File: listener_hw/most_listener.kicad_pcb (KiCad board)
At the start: 2 copper layers, 125 x 80 mm, 169 parts, among them J1 1-1394640-1, J2 ANALYSER, J3 I2S, J4 VBAT_IN, J5 PLR135/T10, J6 PLT133/T10W, J7 RCA 75R, J8 LINE L, J9 LINE R, M1 Tang Nano 20K, M2 ESP32-DevKitC-VIE, U1 74LVC1G34, U10 TPS2553DBVR, U11 74LVC1G123, U12 DIR9001, U13 SRC4192, U14 LP5907MFX-3.3, U15 PCM5102A, U16 LP5907MFX-3.3, U17 OPA1678, U18 TPS60403, U2 74LVC1G157, U3 74LVC1G125, U4 74LVC1G123, U5 TPS7B8133DRV, U6 LMR38020F, U7 Si514, U8 LP5907MFX-3.3, U9 74LVC1G79, X1 24.576MHz

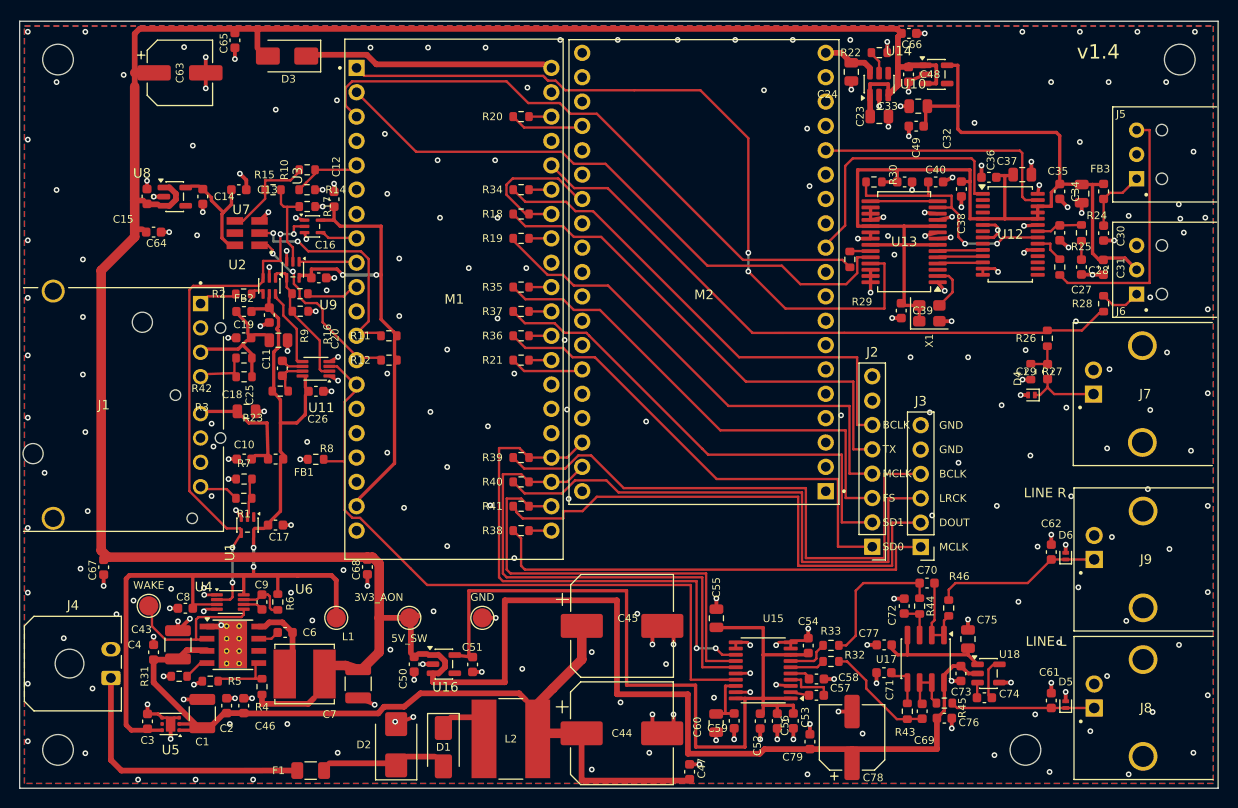
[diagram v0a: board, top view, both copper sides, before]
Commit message: Board v1.4 polished: 6 jumpers (was 9), the user's re-placement routed by hand
The user re-placed 57 parts in rounds: the DIR9001 group packed into three
columns, J2/J3 moved with their bus, the line-out buffer and the power corner
tightened, then R29, R30, R38, R40 and R41. Every net they touched was redrawn
by hand; the autorouter's first pass (25 jumpers) was dropped.

Three jumpers went with it:
- SRC_BCLK: R29 sits where the line crossed under M2, and it runs between its
  pads.
- RST_AIN: from U13.13 through U13's body and under C39/X1 into U12's body.
  U13's 3.3 V links moved outside its body (pins 19/22 left, 10/7 right, C39/X1
  fed from pin 7).
- I2S_BCLK: R39 under M2 by M2.22. The DAC's BCLK comes down through the bodies
  of R40/R41/R38 on top of its bundle, so U15 gets BCLK, DOUT, LRCK in its own
  order.
The U7 knot keeps its three hops, shorter: RX_BUF at the top of its legs,
SI_SCL straight, SI_SDA 1.3 mm.

TP4 (WAKE) is gone from the sheet, the board and gen_listener_pcb.py; WAKE is
probed at R31 or U4. The DevKitC footprint's courtyard is its two pin rows and
the antenna's end: the module sits on headers with room under it.

Board: 6 jumpers, 14 mm of bottom copper, DRC 0/0/0 with schematic parity, ERC
clean. README, the sheet PDF and the fab package follow; sheet and board are
dated 2026-10-02.

Co-Authored-By: Claude Opus 5.5 <noreply@anthropic.com>
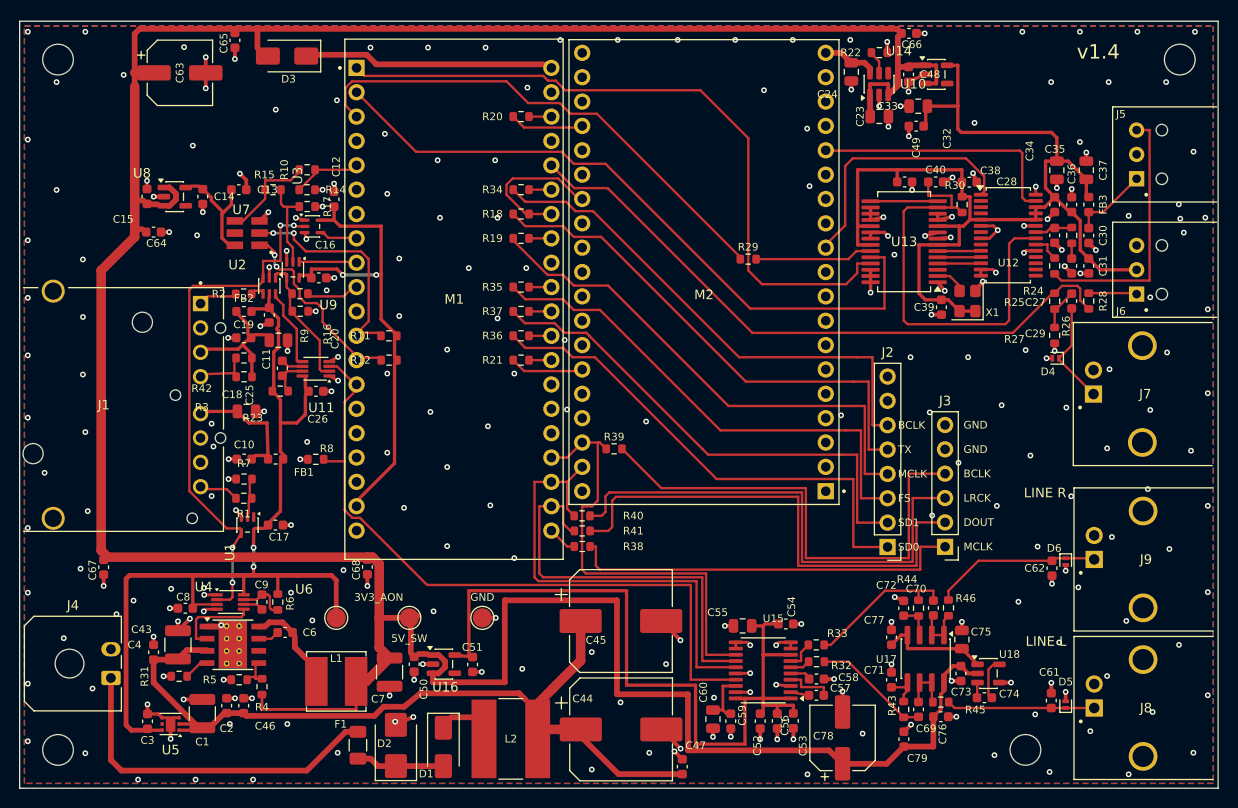
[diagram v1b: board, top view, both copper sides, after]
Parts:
- removed TP4: WAKE, TestPoint:TestPoint_Pad_D2.0mm
- moved R29 10.6 mm to (76.0, 24.8), turned to 180 degrees
- moved C79 9.81 mm to (92.2, 74.9)
- moved R39 9.74 mm to (62.0, 44.6), turned to 0 degrees
- moved R30 9.49 mm to (98.3, 19.1), turned to -90 degrees
- moved C36 9.09 mm to (109.7, 19.1), turned to 90 degrees
- moved C29 7.78 mm to (109.7, 29.2)
- moved R40 7.28 mm to (58.7, 51.6), turned to 0 degrees
- moved R41 6.87 mm to (58.7, 53.2), turned to 0 degrees
- moved C37 6.70 mm to (111.3, 15.5), turned to 90 degrees
- moved R38 6.59 mm to (58.7, 54.8), turned to 0 degrees
- moved F1 5.59 mm to (35.3, 75.5), turned to -90 degrees
- moved D4 4.59 mm to (108.1, 35.2)
- moved R27 4.53 mm to (108.0, 32.8)
- moved C39 4.21 mm to (96.1, 29.8)
- moved X1 4.18 mm to (98.9, 29.2), turned to 90 degrees
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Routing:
- net /RST_AIN: track 26.7 -> 45.3 mm, vias 2 -> 0
- net /I2S_DIN2_F: track 64.4 -> 52.7 mm
- net Net-(U13-SDOUT): track 2.16 -> 12.3 mm
- net Net-(J3-BCLK): track 61.0 -> 51.5 mm
- net /I2S_BCLK_F: track 55.3 -> 45.9 mm, vias 2 -> 0
- net 5V_SW: track 316.4 -> 325.0 mm
- net Net-(J4-VBAT): track 28.4 -> 36.5 mm
- net /WAKE: track 16.5 -> 8.89 mm
- net /SRC_BCLK_F: track 78.6 -> 71.4 mm, vias 2 -> 0
- net /SRC_LRCK_F: track 64.0 -> 71.2 mm
- net 3V3_DA: track 118.5 -> 111.8 mm
- net Net-(J3-MCLK): track 48.2 -> 41.6 mm
- net Net-(J3-LRCK): track 58.0 -> 52.9 mm
- net GND: track 148.3 -> 143.5 mm, vias 275 -> 268
- net 3V3_DAC: track 88.4 -> 84.1 mm
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
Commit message: Board v1.4: 4 jumpers (was 6), the user's last re-placement and the Si514 knot sketch
The user moved the battery corner (F1 by J4, U5 up by U4, L2/D1/D2 left, C43/C2/C46
turned to face U6), U10 and U14 with their capacitors, J2 and J3, and the DAC (U15 and
its capacitors higher, U16 with C50/C51 beside U15, so 3V3_DAC is a short spine under
U15's body); everything re-routed by hand.

- Si514 corner, the user's sketch: RT_CLK takes one jumper under RX_BUF and SI_SCL;
  RX_BUF runs between the Si514's pad rows and over it, CLK+ round its west side, so
  the RX_BUF, SI_SCL and SI_SDA jumpers are gone. SI_SCL dips under 3V3_SW at M1's
  row instead of 3V3_SW jumping SI_SCL.
- C80 (100n), C81 (100u 16V) and C82 (100n 100V): the user's copies on the board, now
  in the sheet; J4's ground stub is shorter so the VBAT_P row takes C82.
- Every junction is a shared vertex; the moved parts' labels are re-placed and J2/J3's
  pin names follow the headers again.

DRC 0 errors, 0 unconnected, 0 differences from the sheet; ERC clean; the copper lint
shows only its accepted set. Sheet PDF and fab/ re-made.

Co-Authored-By: Claude Opus 5.5 <noreply@anthropic.com>
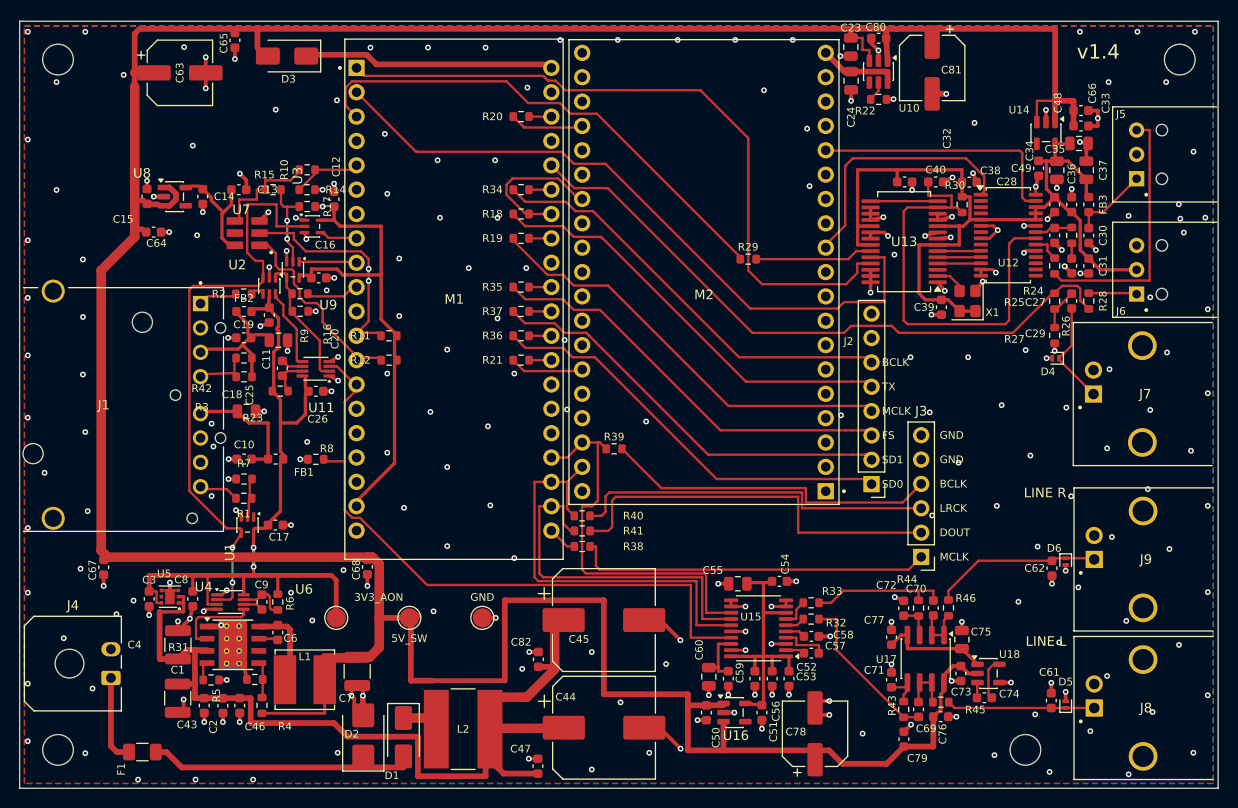
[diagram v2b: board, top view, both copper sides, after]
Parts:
- added C80: 100n, Capacitor_SMD:C_0603_1608Metric, F.Cu at (89.6, 1.78)
- added C81: 100u 16V, Capacitor_SMD:CP_Elec_6.3x7.7, F.Cu at (95.2, 4.88)
- added C82: 100n 100V, Capacitor_SMD:C_0603_1608Metric, F.Cu at (54.1, 66.6)
- moved C50 30.9 mm to (71.6, 72.1)
- moved U16 30.7 mm to (74.5, 72.1)
- moved C51 30.6 mm to (77.4, 72.1)
- moved F1 22.5 mm to (12.8, 76.2), turned to 0 degrees
- moved C66 19.7 mm to (110.7, 9.32)
- moved C48 18.8 mm to (110.7, 10.9), turned to 0 degrees
- moved C33 17.2 mm to (110.5, 12.8), turned to 0 degrees
- moved C47 15.1 mm to (54.1, 77.7)
- moved C49 13.5 mm to (106.3, 15.3), turned to -90 degrees
- moved U5 13.3 mm to (15.7, 60.0)
- moved U14 13.0 mm to (107.0, 11.7), turned to -90 degrees
- moved C3 12.8 mm to (13.5, 60.2), turned to -90 degrees
- moved C23 7.83 mm to (86.7, 2.69), turned to -90 degrees
- moved C43 7.67 mm to (19.3, 71.4), turned to -90 degrees
- moved J2 6.76 mm to (88.8, 48.3)
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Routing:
- net 3V3_DAC: track 84.1 -> 29.9 mm
- net Net-(J4-VBAT): track 36.5 -> 9.24 mm
- net 5V_SW: track 325.0 -> 348.0 mm
- net 3V3_DA: track 111.8 -> 89.2 mm
- net Net-(D1-A): track 9.24 -> 28.8 mm
- net 3V3_AON: track 89.6 -> 71.6 mm
- net Net-(J3-BCLK): track 51.5 -> 35.2 mm
- net Net-(J3-LRCK): track 52.9 -> 38.2 mm
- net Net-(J3-DOUT): track 51.8 -> 41.4 mm
- net Net-(J2-BCLK): track 53.4 -> 44.8 mm
- net Net-(J2-SD0): track 52.3 -> 43.8 mm
- net Net-(J2-UART_TX): track 53.4 -> 44.8 mm
- net Net-(J2-SD1): track 51.9 -> 43.3 mm
- net Net-(J2-MCLK): track 53.5 -> 45.0 mm
- net Net-(J2-FS): track 52.3 -> 43.8 mm
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
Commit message: Board v1.5: 122.5 x 78.9 mm, the user's denser placement routed
The user packed the right and top edges tighter. The outline lost 2.5 mm on
the right and 1.1 mm at the top. The DIR9001 group with U14 moved 1.7 mm
left, J5..J9 and the line-out's output parts 2.4..3.1 mm, the top strip
(U10, C23, C24, C63, C65, C80, C81, D3, R22) 2 mm down. Their copper moved
with them; everything else kept its place and was patched only where a
moved part now sits on it.

- U13: C32, C38 and C40 in one row over its body, R30 under it beside C39
  (the user's sketches). C40.1 drops RST_AIN straight into the U13-U12 gap,
  now 1.1 mm wide, beside the 3.3 V feed that rises from U12.5 to the row's
  rail. U13's ground pins reach vias under its body (the gap has no room).
- DIR9001 group: C36 turned, so C34.2 and C36.2 share one via; the 3.3 V
  riser between C49 and C35.2 necks to 0.25 mm; RXIN in the middle of the
  U12-C28 gap; J5-VOUT between J5/J6's pins and pegs.
- 5V_HOST climbs from C24 to M2.19 between M2's pins and C23/C24; the 5 V
  trunk's top run follows the new edge; VBAT_P by U6 back on its old riser.
- Lock flags of the carried copper restored; 15 stitching vias along the
  new edges and the moved holes H1, H2, H4; 20 labels re-placed.

Still 4 jumpers, 9 mm of bottom copper, 251 vias. DRC 0 errors, nothing
unconnected, no difference from the sheet; ERC 0; no T-ends or crossings in
the copper; no silk overlap that v1.4 did not have. The sheet changes only
in its title block (rev 1.5, 2026-10-03); its PDF and fab/ are rewritten
from it and the board. README: size, the v1.5 round, four M3 holes (it said
six).

Co-Authored-By: Claude Opus 5.5 <noreply@anthropic.com>
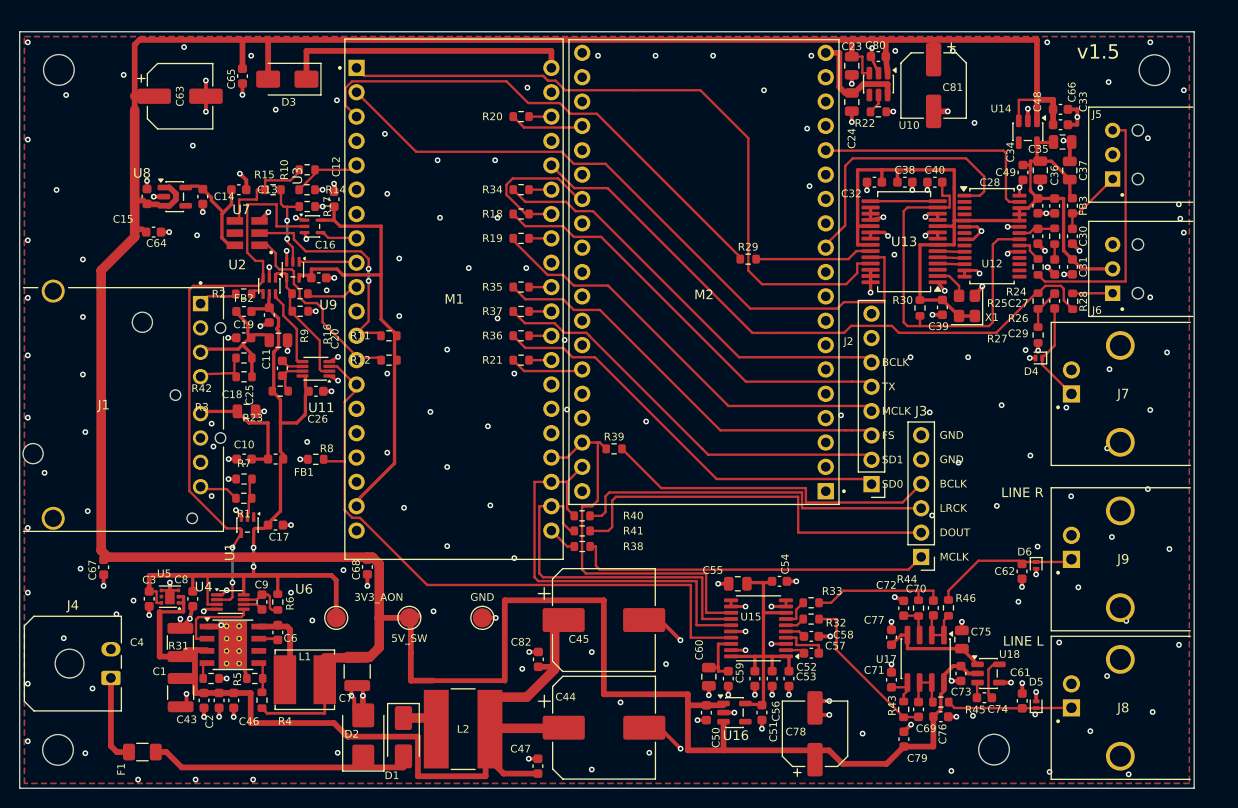
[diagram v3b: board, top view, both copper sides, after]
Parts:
- moved R30 11.6 mm to (93.9, 29.9)
- moved C38 6.72 mm to (92.3, 16.8)
- moved C65 3.82 mm to (23.2, 5.73)
- moved H4 3.28 mm to (101.6, 76.0)
- moved C32 3.15 mm to (89.2, 16.8), turned to 180 degrees
- moved C62 3.14 mm to (104.5, 57.4)
- moved D6 3.10 mm to (106.0, 56.7)
- moved D5 3.08 mm to (106.0, 71.3)
- moved C61 3.03 mm to (104.6, 70.9)
- moved H2 2.86 mm to (118.4, 5.11)
- moved J6 2.50 mm to (114.0, 25.8)
- moved J5 2.50 mm to (114.0, 13.9)
- moved C63 2.44 mm to (16.7, 7.82)
- moved D3 2.41 mm to (27.9, 6.05)
- moved J9 2.37 mm to (109.7, 56.1)
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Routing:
- net Net-(D3-K): track 24.0 -> 30.3 mm
- net /RST_AIN: track 45.3 -> 41.8 mm
- net /5V_HOST: track 8.40 -> 11.8 mm
- net 5V_SW: track 348.0 -> 350.6 mm
- net Net-(D5-A1): track 15.4 -> 13.1 mm
- net Net-(D6-A1): track 17.6 -> 15.4 mm
- net /OPT_NPCM: track 26.7 -> 28.5 mm
- net Net-(U12-DOUT): track 4.50 -> 2.80 mm
- net Net-(U12-LRCKO): track 4.50 -> 2.80 mm
- net Net-(U12-BCKO): track 4.50 -> 2.80 mm
- net GND: track 150.6 -> 148.9 mm, vias 256 -> 243
- net /SPDIF_F: track 67.6 -> 66.0 mm
- net /OPT_ERR: track 26.8 -> 25.2 mm
- net 3V3_DA: track 89.2 -> 88.2 mm
- net Net-(J6-VIN): track 5.04 -> 4.17 mm
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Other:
- board size 125 x 80 mm -> 122.5 x 78.9 mm
- board text added: "v1.5"
- board text removed: "v1.4"
